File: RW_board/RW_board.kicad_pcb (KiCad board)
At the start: 4 copper layers, 45.6 x 45.6 mm, 129 parts, among them IC201 MAX44284WAUT+T, IC301 MCT8316Z0RQRGFRQ1, J1 Conn_01x08_Pin, J2 1-84953-1, J401 USB4105-GF-A, J402 20021521-00010T4LF, Q201 BSZ300N15NS5ATMA1, SW401 SW_Push, U201 LM5022MM, U401 ATSAMD21G18A-M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

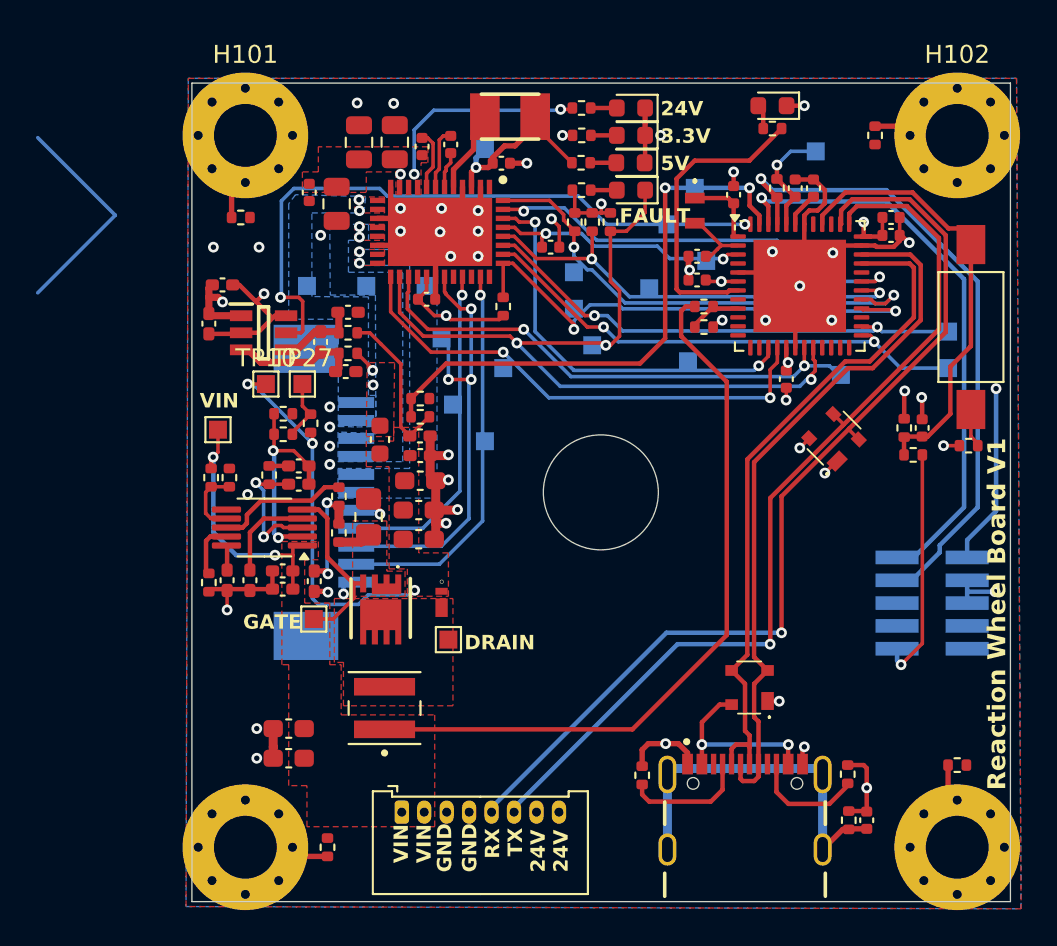
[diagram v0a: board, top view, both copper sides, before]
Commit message: Curr Sense Edits & 24V Reroute
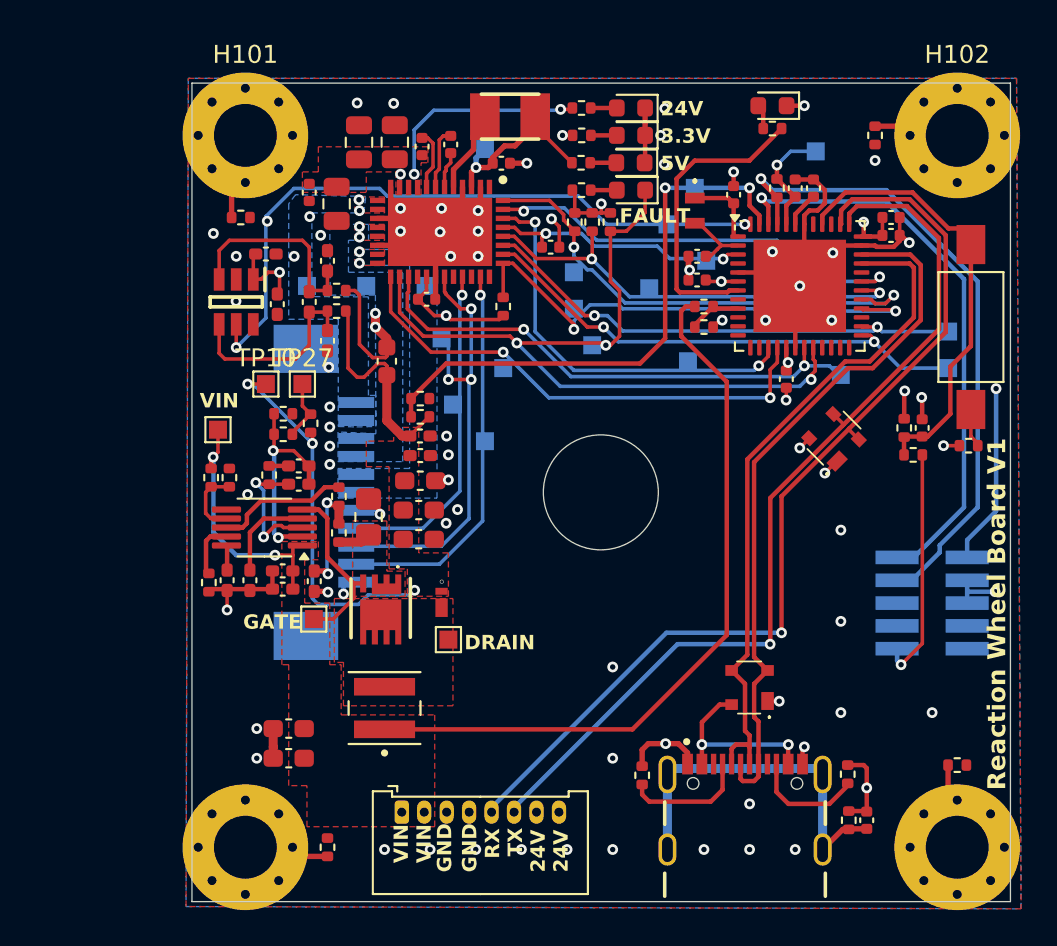
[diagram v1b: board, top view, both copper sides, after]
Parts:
- moved C218 6.25 mm to (134.0, 86.6), turned to 90 degrees
- moved R213 4.38 mm to (137.3, 92.2)
- moved C210 3.96 mm to (131.2, 89.0)
- moved R214 3.55 mm to (134.5, 88.3)
- moved C1 2.96 mm to (130.6, 86.2)
- moved C217 2.32 mm to (133.0, 88.9), turned to 90 degrees
- moved IC201 2.30 mm to (128.9, 88.9), turned to -90 degrees
- moved C216 1.95 mm to (134.0, 91.1), turned to -90 degrees
- moved R212 1.37 mm to (134.5, 89.4)
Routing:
- net GND: track 105.2 -> 88.2 mm, vias 50 -> 72
- net Net-(D201-K): track 43.1 -> 33.8 mm
- net /Buck-Boost/24V_OUT: track 13.0 -> 19.9 mm
- net /Buck-Boost/Sense-: track 4.55 -> 11.0 mm
- net /Buck-Boost/Sense+: track 7.09 -> 11.6 mm
- net /Buck-Boost/CURRENTSENSE: track 36.6 -> 37.7 mm, vias 2 -> 3
- net unconnected-(J2-PadMP2): vias 0 -> 1

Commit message: Changed Footprints
Hand Solder to not
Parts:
- C1, C203, C204, C205, C206, C207, C208, C209, C210, C214, C215, C216, C217, C218: footprint Capacitor_SMD:C_0402_1005Metric_Pad0.74x0.62mm_HandSolder -> Capacitor_SMD:C_0402_1005Metric
- C201, C202, C211, C212, C213: footprint Capacitor_SMD:C_0603_1608Metric_Pad1.08x0.95mm_HandSolder -> Capacitor_SMD:C_0603_1608Metric
- D201: footprint RW_Imports:X3-WLB1608-2 -> Senior Design:X3-WLB1608-2
- D401, D403: footprint RW_Imports:PRTR5V0U2X -> Senior Design:PRTR5V0U2X
- IC201: footprint RW_Imports:SOT95P280X145-6N -> Senior Design:SOT95P280X145-6N
- IC301: footprint RW_Imports:QFN50P500X700X100-41N-D -> Senior Design:QFN50P500X700X100-41N-D
- J2: footprint RW_Imports:1849531 -> Senior Design:1849531
- J402: footprint RW_Imports:2002152100010T4LF -> Senior Design:2002152100010T4LF
- Q201: footprint RW_Imports:BSZ300N15NS5ATMA1 -> Senior Design:BSZ300N15NS5ATMA1
- R207: footprint Resistor_SMD:R_0805_2012Metric_Pad1.20x1.40mm_HandSolder -> Resistor_SMD:R_0805_2012Metric
- Y401: footprint RW_Imports:830105946101 -> Senior Design:830105946101
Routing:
- net unconnected-(J2-PadMP2): vias 1 -> 0
- net /Buck-Boost/CURRENTSENSE: vias 3 -> 2

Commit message: Bom completed and generated, minor PCB adjustments
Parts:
- C309: footprint Capacitor_SMD:C_0402_1005Metric -> Capacitor_SMD:C_0805_2012Metric
- R213: footprint Capacitor_SMD:C_0603_1608Metric -> Resistor_SMD:R_0603_1608Metric
- R306, R307, R309, R406: value 330 -> 330R
- moved C309 2.92 mm to (146.5, 81.9), turned to -90 degrees
- moved R309 0.34 mm to (148.5, 82.6)
- moved R306 0.30 mm to (148.4, 81.2)
- moved R302 0.08 mm to (147.8, 84.5)
- renumbered C1 to C219
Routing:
- net /Motor Driver/FB_BK: track 15.6 -> 16.6 mm
- net GND: track 88.2 -> 87.3 mm
